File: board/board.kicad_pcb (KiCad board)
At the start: 4 copper layers, 100 x 100 mm, 49 parts, among them J1 UART, J2 USB_B, Q2 Q_NPN_BEC, SW1 SW_SPST, SW2 SW_SPST, SW4 SW_SPST, U1 4040, U2 NE555D, U3 4040, U4 LM741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

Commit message: add: vias through - fix: routes
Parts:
- removed C12, C13, C14, C15: 100pF, Capacitor_SMD:C_0201_0603Metric
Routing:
- net DT-: track 23.0 -> 17.5 mm, vias 2 -> 0
- net DT+: track 23.2 -> 18.2 mm, vias 2 -> 0
- net Net-(BZ1--): track 33.2 -> 35.3 mm
- net ALARM: track 50.9 -> 52.3 mm
- net GND: track 50.0 -> 51.3 mm, vias 30 -> 27
- net 5V: track 82.9 -> 81.7 mm, vias 28 -> 23
- net CLOCK: track 34.9 -> 34.1 mm

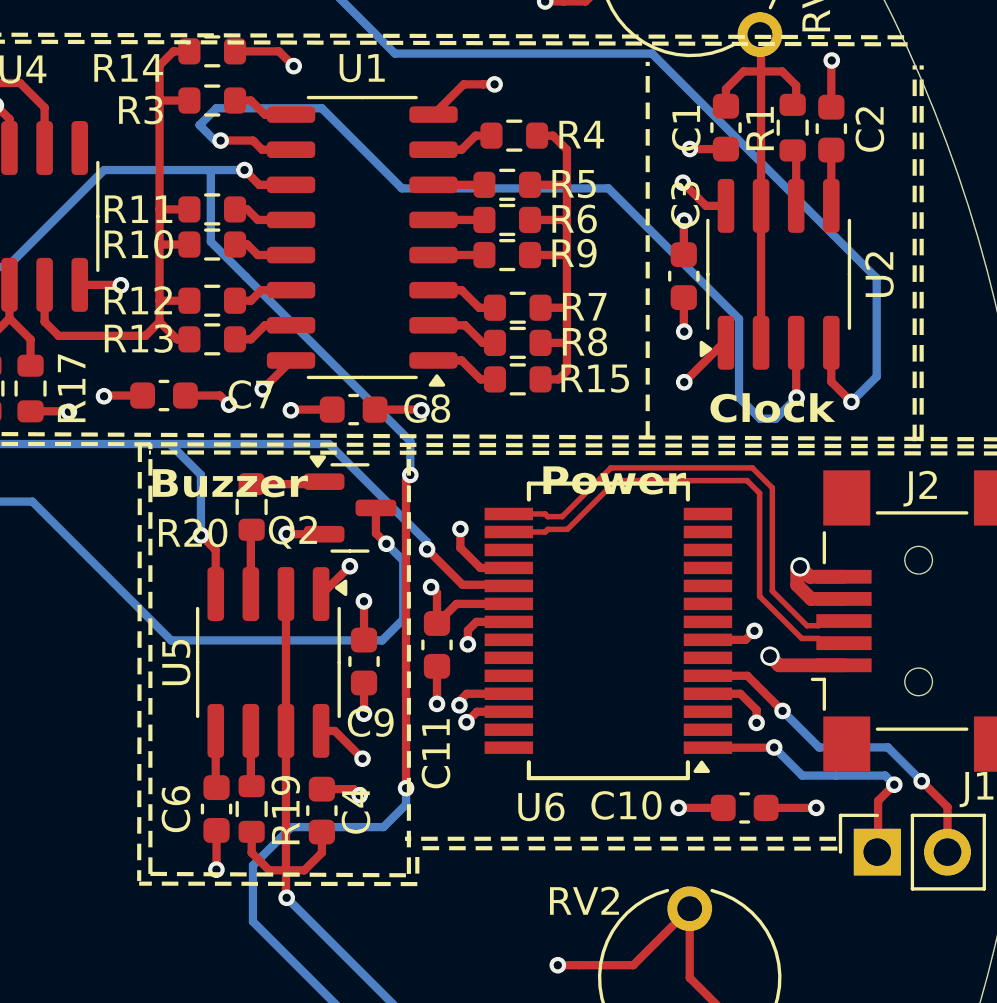
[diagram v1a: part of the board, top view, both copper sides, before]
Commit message: add: stitching capacitor & gerbers
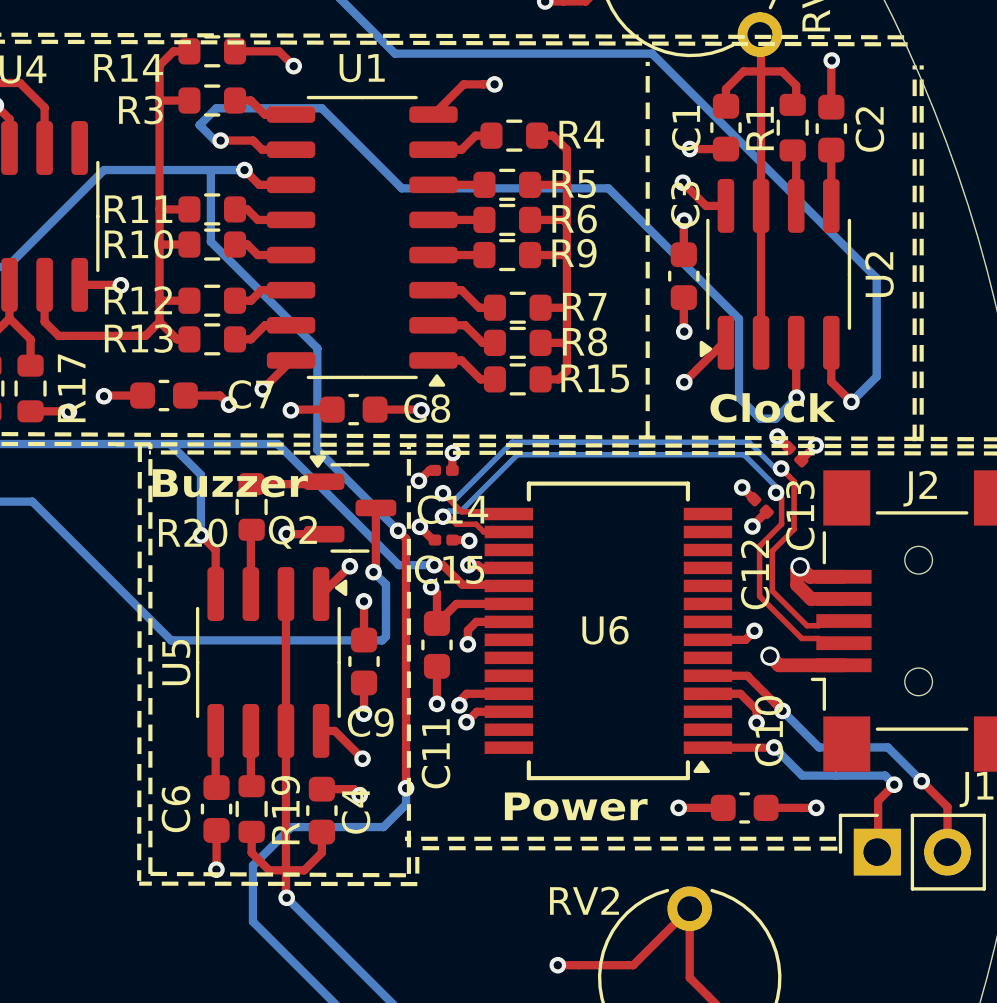
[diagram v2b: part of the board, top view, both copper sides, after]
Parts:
- added C12: 100pF, Capacitor_SMD:C_0201_0603Metric, F.Cu at (111.0, 64.3)
- added C13: 100pF, Capacitor_SMD:C_0201_0603Metric, F.Cu at (112.3, 62.4)
- added C14: 100pF, Capacitor_SMD:C_0201_0603Metric, F.Cu at (99.5, 63.0)
- added C15: 100pF, Capacitor_SMD:C_0201_0603Metric, F.Cu at (99.6, 65.5)
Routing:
- net DT+: track 18.2 -> 25.0 mm, vias 0 -> 2
- net DT-: track 17.5 -> 24.2 mm, vias 0 -> 2
- net 5V: track 81.7 -> 84.4 mm, vias 23 -> 27
- net GND: track 51.3 -> 52.9 mm, vias 27 -> 31

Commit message: add: pcb layout & gerbers
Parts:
- added H1: MountingHole, MountingHole:MountingHole_3.2mm_M3, F.Cu at (50.0, 55.2)
- added H2: MountingHole, MountingHole:MountingHole_3.2mm_M3, F.Cu at (70.0, 95.0)
- moved C15 0.73 mm to (98.8, 65.4), turned to -45 degrees
- moved C14 0.67 mm to (98.9, 63.2), turned to 45 degrees
- moved C12 0.40 mm to (110.6, 64.3), turned to -90 degrees
- moved C13 0.32 mm to (112.3, 62.1)
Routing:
- net 5V: track 84.4 -> 85.1 mm, vias 27 -> 26

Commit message: add: Referencias en Silkscreen centradas al componente
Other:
- board text added: "BZ1"
- board text added: "J2"
- board text added: "RV1"
- board text added: "RV2"
- board text added: "SW1"
- board text added: "SW2"
- board text added: "SW4"
- board text added: "U1"
- board text added: "U2"
- board text added: "U3"
- board text added: "U4"
- board text added: "U5"
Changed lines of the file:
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@@
+		)
+	)
+	(gr_text "SW1"
+		(at 72.2884 24.0284 0)
+		(layer "F.SilkS")
+		(effects
+			(font
+				(size 1 1)
+				(thickness 0.15)
+			)
+		)
+	)
+	(gr_text "U1"
+		(at 96.612 54.61 0)
+		(layer "F.SilkS")
+		(effects
+			(font
+				(size 1 1)
+				(thickness 0.15)
+			)
+		)
+	)
+	(gr_text "U4"
+		(at 84.425 53.848 0)
+		(layer "F.SilkS")
+		(effects
+			(font
+				(size 1 1)
+				(thickness 0.15)
+			)
+		)
+	)
+	(gr_text "J2"
+		(at 117.54 68.4784 0)
+		(layer "F.SilkS")
+		(effects
+			(font
+				(size 1 1)
+				(thickness 0.15)
+			)
+		)
+	)
+	(gr_text "SW4"
+		(at 108.1024 92.0496 0)
+		(layer "F.SilkS")
+		(effects
+			(font
+				(size 1 1)
+				(thickness 0.15)
+			)
+		)
+	)
+	(gr_text "U3"
+		(at 76.743 54.483 0)
+		(layer "F.SilkS")
+		(effects
+			(font
+				(size 1 1)
+				(thickness 0.15)
+			)
+		)
+	)
+	(gr_text "U5"
+		(at 93.283 69.977 0)
+		(layer "F.SilkS")
+		(effects
+			(font
+				(size 1 1)
+				(thickness 0.15)
+			)
+		)
+	)
+	(gr_text "SW2"
+		(at 33.7312 91.9988 0)
+		(layer "F.SilkS")
+		(effects
+			(font
+				(size 1 1)
+				(thickness 0.15)
+			)
+		)
+	)
+	(gr_text "RV1"
+		(at 108.493 44.766 0)
+		(layer "F.SilkS")
+		(effects
+			(font
+				(size 1 1)
+				(thickness 0.15)
+			)
+		)
+	)
+	(gr_text "U2"
+		(at 111.603 55.942 0)
+		(layer "F.SilkS")
+		(effects
+			(font
+				(size 1 1)
+				(thickness 0.15)
+			)
+		)
+	)
+	(gr_text "BZ1"
+		(at 71 68.5 0)
+		(layer "F.SilkS")
+		(effects
+			(font
+				(size 1 1)
+				(thickness 0.15)
+			)
 		)
 	)
@@
 		)
 	)
+	(gr_text "RV2"
+		(at 108.33 81.91 0)
+		(layer "F.SilkS")
+		(effects
+			(font
+				(size 1 1)
+				(thickness 0.15)
+			)
+		)
+	)

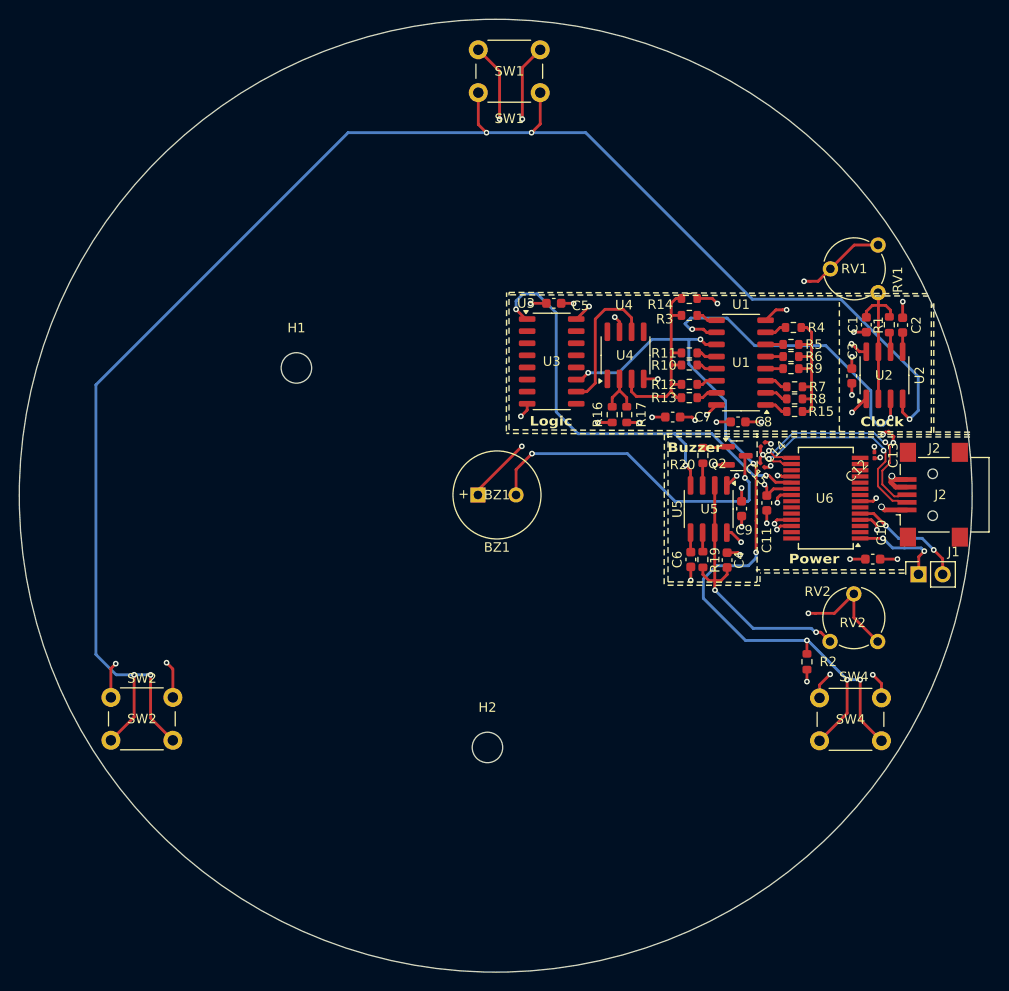
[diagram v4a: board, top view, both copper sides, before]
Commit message: add: 3 mechanical holes & .step 3d
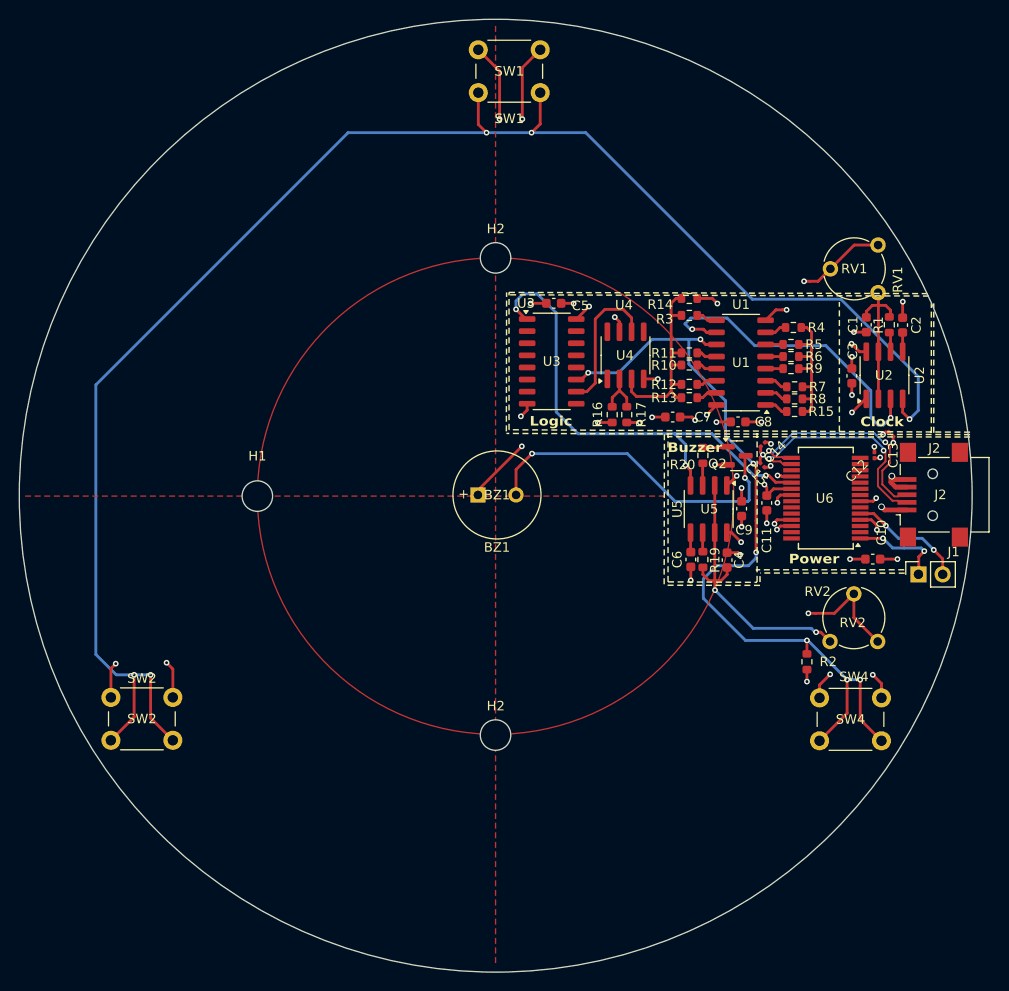
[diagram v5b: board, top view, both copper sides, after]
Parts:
- added H2: MountingHole, MountingHole:MountingHole_3.2mm_M3, F.Cu at (70.8, 43.6)
- moved H1 14.1 mm to (45.9, 68.6)
- moved H2 1.55 mm to (70.8, 93.7)
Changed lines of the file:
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@@
 		)
 	)
+	(footprint "MountingHole:MountingHole_3.2mm_M3"
+		(layer "F.Cu")
+		(at 70.85 43.62)
+		(descr "Mounting Hole 3.2mm, no annular, M3")
+		(tags "mounting hole 3.2mm no annular m3")
+		(property "Reference" "H2"
+			(at 0.02 -3.05 0)
+			(layer "F.SilkS")
+			(effects
+				(font
+					(size 1 1)
+					(thickness 0.15)
+				)
+			)
+		)
+		(property "Value" "MountingHole"
+			(at 0 4.2 0)
+			(layer "F.Fab")
+			(effects
+				(font
+					(size 1 1)
+					(thickness 0.15)
+				)
+			)
+		)
+		(property "Datasheet" ""
+			(at 0 0 0)
+			(unlocked yes)
+			(layer "F.Fab")
+			(hide yes)
+			(effects
+				(font
+					(size 1.27 1.27)
+					(thickness 0.15)
+				)
+			)
+		)
+		(property "Description" "Mounting Hole without connection"
+			(at 0 0 0)
+			(unlocked yes)
+			(layer "F.Fab")
+			(hide yes)
+			(effects
+				(font
+					(size 1.27 1.27)
+					(thickness 0.15)
+				)
+			)
+		)
+		(attr exclude_from_pos_files exclude_from_bom)
+		(fp_circle
+			(center 0 0)
+			(end 3.2 0)
+			(stroke
+				(width 0.15)
+				(type solid)
+			)
+			(fill no)
+			(layer "Cmts.User")
+		)
+		(fp_circle
+			(center 0 0)
+			(end 3.45 0)
+			(stroke
+				(width 0.05)
+				(type solid)
+			)
+			(fill no)
+			(layer "F.CrtYd")
+		)
+		(fp_text user "${REFERENCE}"
+			(at 0 0 0)
+			(layer "F.Fab")
+			(effects
+				(font
+					(size 1 1)
+					(thickness 0.15)
+				)
+			)
+		)
+		(pad "" np_thru_hole circle
+			(at 0 0)
+			(size 3.2 3.2)
+			(drill 3.2)
+			(layers "*.Cu" "*.Mask")
+		)
+		(embedded_fonts no)
+	)
 	(footprint "Capacitor_SMD:C_0603_1608Metric"
 		(layer "F.Cu")
@@
 	(footprint "MountingHole:MountingHole_3.2mm_M3"
 		(layer "F.Cu")
-		(at 70 95)
+		(at 70.85 93.7)
 		(descr "Mounting Hole 3.2mm, no annular, M3")
 		(tags "mounting hole 3.2mm no annular m3")
 		(property "Reference" "H2"
-			(at 0 -4.2 0)
+			(at 0.02 -3.05 0)
 			(layer "F.SilkS")
 			(effects
@@
 	(footprint "MountingHole:MountingHole_3.2mm_M3"
 		(layer "F.Cu")
-		(at 49.95 55.17)
+		(at 45.85 68.62)
 		(descr "Mounting Hole 3.2mm, no annular, M3")
 		(tags "mounting hole 3.2mm no annular m3")
@@
 		(embedded_fonts no)
 		(model "${KICAD9_3DMODEL_DIR}/Button_Switch_THT.3dshapes/SW_PUSH_6mm_H4.3mm.wrl"
+			(hide yes)
+			(offset
+				(xyz 0 0 0)
+			)
+			(scale
+				(xyz 1 1 1)
+			)
+			(rotate
+				(xyz 0 0 0)
+			)
+		)
+		(model "${KICAD9_3DMODEL_DIR}/Button_Switch_THT.3dshapes/SW_PUSH_6mm_H9.5mm.wrl"
 			(offset
 				(xyz 0 0 0)
@@
 		)
 	)
+	(gr_circle
+		(center 70.85 68.62)
+		(end 95.85 68.62)
+		(stroke
+			(width 0.1)
+			(type dot)
+		)
+		(fill no)
+		(layer "F.Cu")
+		(net 4)
+	)
+	(gr_line
+		(start 70.85 19.27)
+		(end 70.85 117.96)
+		(stroke
+			(width 0.1)
+			(type dot)
+		)
+		(layer "F.Cu")
+	)
+	(gr_line
+		(start 88.6 68.62)
+		(end 21.38989 68.62)
+		(stroke
+			(width 0.1)
+			(type dot)
+		)
+		(layer "F.Cu")
+	)
 	(gr_line
